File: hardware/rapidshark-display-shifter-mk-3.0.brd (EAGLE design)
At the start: 21 x 21 mm, 15 parts, among them Q1 IRLML2502, Q2 IRLML2502

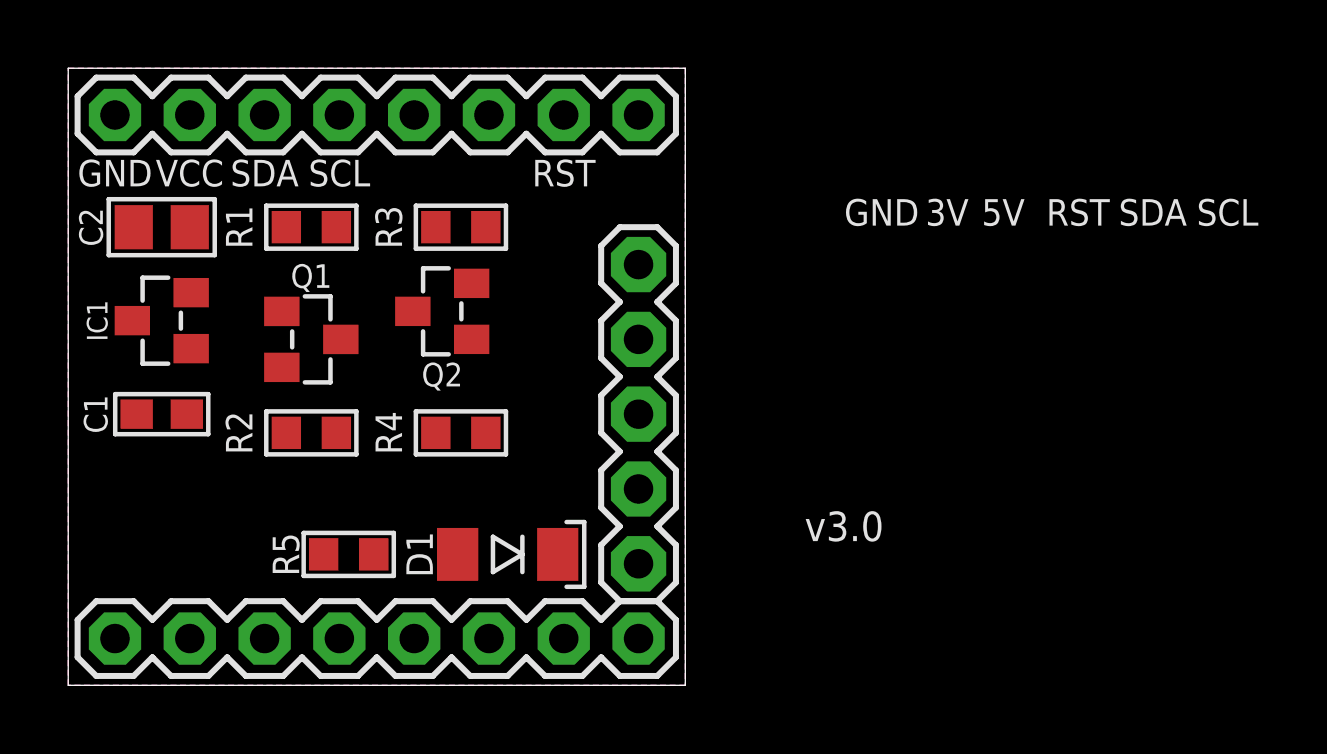
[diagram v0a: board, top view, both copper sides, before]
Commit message: layout for sf butt adapter complete
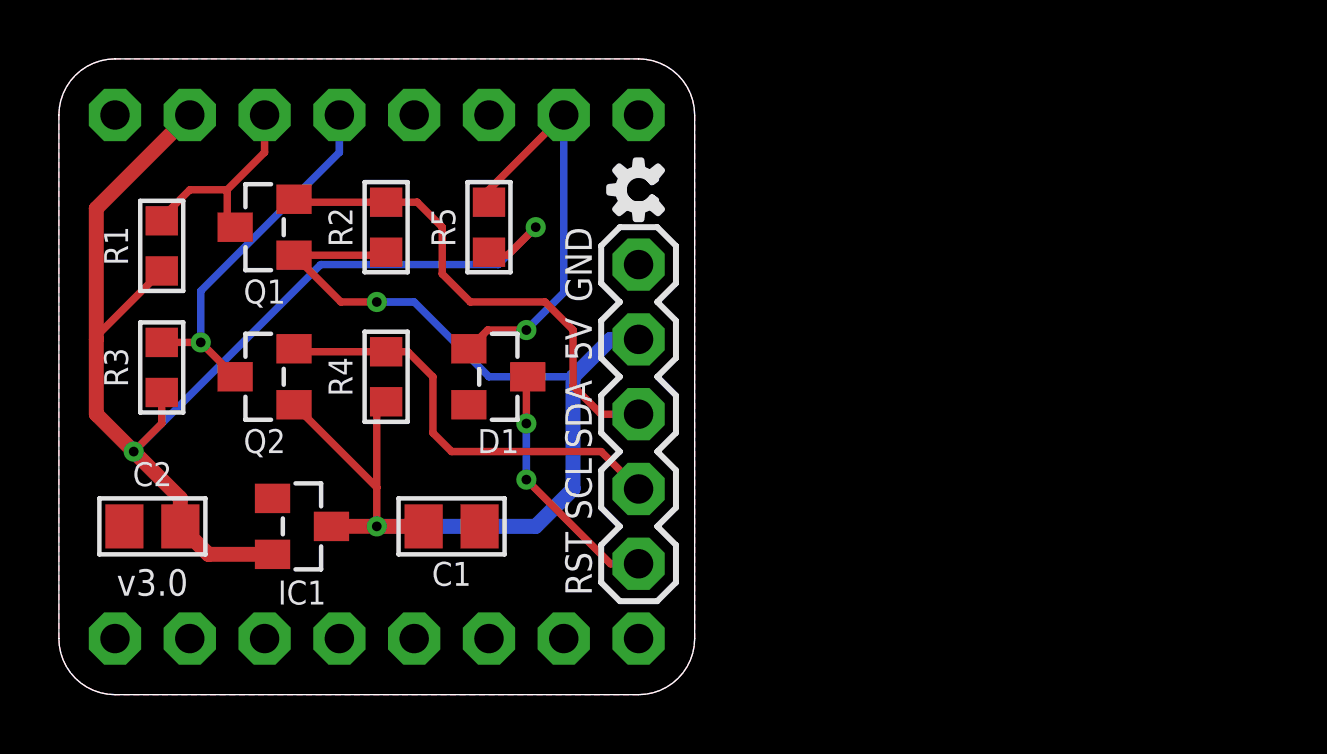
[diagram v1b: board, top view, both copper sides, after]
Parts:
- added U$1: (no value), A_butts:COW_SMALL
- added U$2, U$3: (no value), A_butts:OSHWLOGO_TINY_SILKONLY
- C1: device A_butts:C0603 -> A_butts:C0805
- D1: value (none) -> BAS19L; device A_butts:SOD80C -> A_butts:SOT23
- IC1: value (none) -> AP2210N-3.3V
- JP2, JP3: value (none) -> M081X08
- moved R5 12.1 mm to (14.0, 15.2), turned to 90 degrees
- moved R3 11.2 mm to (2.86, 10.5), turned to 90 degrees
- moved C1 10.6 mm to (12.7, 5.08)
- moved C2 10.2 mm to (2.54, 5.08)
- moved IC1 8.45 mm to (7.62, 5.08), turned to 270 degrees
- moved R2 7.43 mm to (10.5, 15.2), turned to 90 degrees
- moved Q2 6.43 mm to (6.35, 10.2)
- moved D1 6.04 mm to (14.3, 10.2), turned to 270 degrees
- moved R1 5.12 mm to (2.86, 14.6), turned to 90 degrees
- moved Q1 4.13 mm to (6.35, 15.2), turned to 90 degrees
- moved R4 3.17 mm to (10.5, 10.2), turned to 90 degrees
- flipped JP2 to the bottom, turned to 180 degrees
- flipped JP3 to the bottom, turned to 180 degrees
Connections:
- net DISP-RST-IN: now also D1.3; no longer D1.C
- net DISP-RST-OUT: now also D1.1; no longer D1.A
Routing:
- net 3.3V: track 0.00 -> 44.5 mm, vias 0 -> 2
- net 5V: track 0.00 -> 39.6 mm, vias 0 -> 2
- net SDA-IN: track 0.00 -> 16.8 mm
- net SCL-IN: track 0.00 -> 14.8 mm
- net DISP-RST-OUT: track 0.00 -> 14.1 mm, vias 0 -> 1
- net SCL-OUT: track 0.00 -> 12.6 mm, vias 0 -> 1
- net DISP-RST-IN: track 0.00 -> 8.51 mm, vias 0 -> 2
- net SDA-OUT: track 0.00 -> 7.17 mm
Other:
- board size 21 x 21 mm -> 21.6 x 21.6 mm
- board text added: "2"
- board text added: "OLED I C Adapter 3.3V <-> 5V"
- board text added: "by schizobovine <sean@yak.net>"
- board text removed: "3V"
